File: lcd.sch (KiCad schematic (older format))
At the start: 1 part

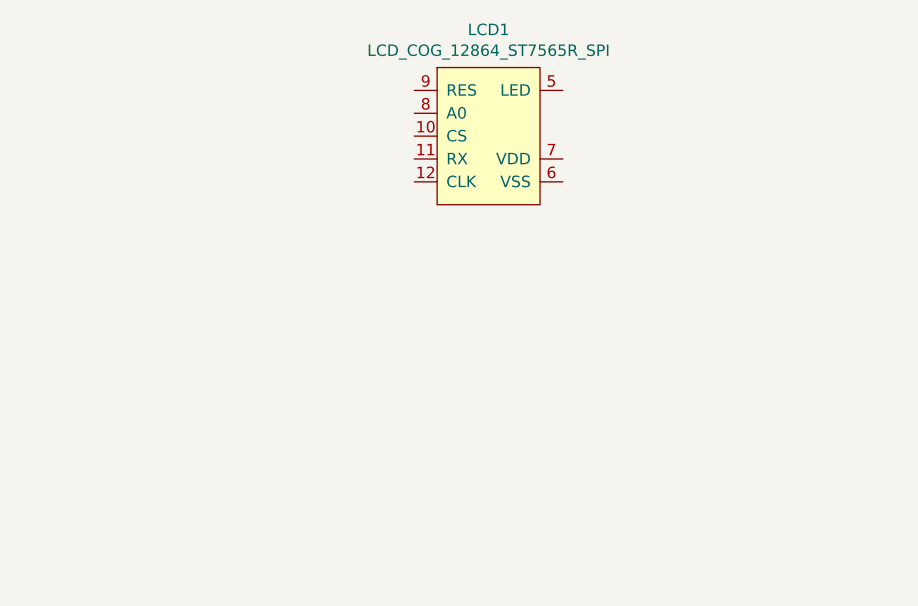
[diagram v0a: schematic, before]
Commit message: dcdc доделан на 5V.
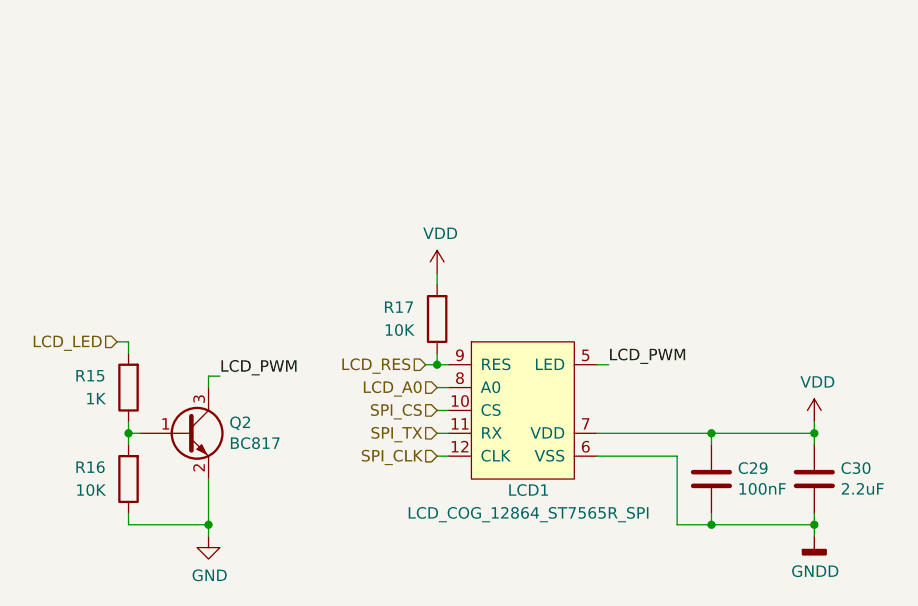
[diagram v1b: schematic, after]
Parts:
- added C29: 100nF, Capacitor_SMD:C_0603_1608Metric_Pad1.05x0.95mm_HandSolder, symbol Device:C
- added C30: 2.2uF, Capacitor_SMD:C_1206_3216Metric_Pad1.42x1.75mm_HandSolder, symbol Device:C
- added Q2: BC817, Package_TO_SOT_SMD:SOT-23, symbol Transistor_BJT:BC817
- added R15: 1K, Resistor_SMD:R_0603_1608Metric_Pad1.05x0.95mm_HandSolder, symbol Device:R
- added R16, R17: 10K, Resistor_SMD:R_0603_1608Metric_Pad1.05x0.95mm_HandSolder, symbol Device:R
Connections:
- net SPI_CS: now reaches LCD1.10 (CS)
- net SPI_TX: now reaches LCD1.11 (RX)
- net SPI_CLK: now reaches LCD1.12 (CLK)
- net LCD_PWM: now reaches LCD1.5 (LED)
- net LCD_PWM: now also Q2.3 (C)
- net GNDD: now reaches LCD1.6 (VSS)
- net GNDD: now also C29.2, C30.2
- net VDD: now reaches LCD1.7 (VDD)
- net VDD: now also C29.1, C30.1, R17.2
- net LCD_A0: now reaches LCD1.8 (A0)
- net LCD_RES: now reaches LCD1.9 (RES)
- net LCD_RES: now also R17.1
- new net: Q2.1 (B), R15.1, R16.2
- new net GND: Q2.2 (E), R16.1
- new net LCD_LED: R15.2
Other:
- moved on the sheet: LCD1
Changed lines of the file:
@@
 L lcd:LCD_COG_12864_ST7565R_SPI LCD1
 U 1 1 5E9E07DE
-P 5850 2700
-F 0 "LCD1" H 5825 3165 50  0000 C CNN
-F 1 "LCD_COG_12864_ST7565R_SPI" H 5825 3074 50  0000 C CNN
-F 2 "lcd:LCD_COG_12864_ST7565R" H 5850 3050 50  0001 C CNN
-F 3 "" H 5850 3050 50  0001 C CNN
-	1    5850 2700
-	1    0    0    -1
-$EndComp
+P 6000 3900
+F 0 "LCD1" H 6000 3550 50  0000 C CNN
+F 1 "LCD_COG_12864_ST7565R_SPI" H 6000 3450 50  0000 C CNN
+F 2 "lcd:LCD_COG_12864_ST7565R" H 6000 4250 50  0001 C CNN
+F 3 "" H 6000 4250 50  0001 C CNN
+	1    6000 3900
+	1    0    0    -1
+$EndComp
+$Comp
+L Device:R R?
+U 1 1 5EA8F117
+P 4250 3800
+AR Path="/5EBBB05A/5EA8F117" Ref="R?"  Part="1"
+AR Path="/5E9E00DA/5EA8F117" Ref="R15"  Part="1"
+F 0 "R15" H 4350 3750 50  0000 L CNN
+F 1 "1K" H 4350 3850 50  0000 L CNN
+F 2 "Resistor_SMD:R_0603_1608Metric_Pad1.05x0.95mm_HandSolder" V 4180 3800 50  0001 C CNN
+F 3 "~" H 4250 3800 50  0001 C CNN
+	1    4250 3800
+	-1   0    0    1
+$EndComp
+$Comp
+L Device:R R?
+U 1 1 5EA8F11D
+P 4250 4200
+AR Path="/5EBBB05A/5EA8F11D" Ref="R?"  Part="1"
+AR Path="/5E9E00DA/5EA8F11D" Ref="R16"  Part="1"
+F 0 "R16" H 4350 4150 50  0000 L CNN
+F 1 "10K" H 4350 4250 50  0000 L CNN
+F 2 "Resistor_SMD:R_0603_1608Metric_Pad1.05x0.95mm_HandSolder" V 4180 4200 50  0001 C CNN
+F 3 "~" H 4250 4200 50  0001 C CNN
+	1    4250 4200
+	-1   0    0    1
+$EndComp
+$Comp
+L Transistor_BJT:BC817 Q?
+U 1 1 5EA8F129
+P 4500 4000
+AR Path="/5EBBB05A/5EA8F129" Ref="Q?"  Part="1"
+AR Path="/5E9E00DA/5EA8F129" Ref="Q2"  Part="1"
+F 0 "Q2" H 4691 4046 50  0000 L CNN
+F 1 "BC817" H 4691 3955 50  0000 L CNN
+F 2 "Package_TO_SOT_SMD:SOT-23" H 4700 3925 50  0001 L CIN
+F 3 "http://www.fairchildsemi.com/ds/BC/BC817.pdf" H 4500 4000 50  0001 L CNN
+	1    4500 4000
+	1    0    0    -1
+$EndComp
+Wire Wire Line
+	4300 4000 4250 4000
+Wire Wire Line
+	4250 4000 4250 3950
+Wire Wire Line
+	4250 4050 4250 4000
+Connection ~ 4250 4000
+$Comp
+L power:GND #PWR?
+U 1 1 5EA8F142
+P 4600 4450
+AR Path="/5EBBB05A/5EA8F142" Ref="#PWR?"  Part="1"
+AR Path="/5E9E00DA/5EA8F142" Ref="#PWR042"  Part="1"
+F 0 "#PWR042" H 4600 4200 50  0001 C CNN
+F 1 "GND" H 4605 4277 50  0000 C CNN
+F 2 "" H 4600 4450 50  0001 C CNN
+F 3 "" H 4600 4450 50  0001 C CNN
+	1    4600 4450
+	1    0    0    -1
+$EndComp
+Wire Wire Line
+	4600 4200 4600 4400
+Wire Wire Line
+	4250 4350 4250 4400
+Wire Wire Line
+	4200 3600 4250 3600
+Wire Wire Line
+	4250 3600 4250 3650
+Wire Wire Line
+	4250 4400 4600 4400
+Wire Wire Line
+	4600 4400 4600 4450
+Connection ~ 4600 4400
+$Comp
+L Device:R R?
+U 1 1 5EA8F3E7
+P 5600 3500
+AR Path="/5EBBB05A/5EA8F3E7" Ref="R?"  Part="1"
+AR Path="/5E9E00DA/5EA8F3E7" Ref="R17"  Part="1"
+F 0 "R17" H 5700 3450 50  0000 L CNN
+F 1 "10K" H 5700 3550 50  0000 L CNN
+F 2 "Resistor_SMD:R_0603_1608Metric_Pad1.05x0.95mm_HandSolder" V 5530 3500 50  0001 C CNN
+F 3 "~" H 5600 3500 50  0001 C CNN
+	1    5600 3500
+	-1   0    0    1
+$EndComp
+Wire Wire Line
+	5600 3650 5600 3700
+Wire Wire Line
+	5600 3700 5650 3700
+Wire Wire Line
+	5600 3700 5550 3700
+Connection ~ 5600 3700
+Text HLabel 5550 3700 0    50   Input ~ 0
+LCD_RES
+Text HLabel 5600 3800 0    50   Input ~ 0
+LCD_A0
+Text HLabel 5600 4000 0    50   Input ~ 0
+SPI_TX
+Text HLabel 5600 4100 0    50   Input ~ 0
+SPI_CLK
+Text HLabel 5600 3900 0    50   Input ~ 0
+SPI_CS
+Wire Wire Line
+	5600 3800 5650 3800
+Wire Wire Line
+	5650 3900 5600 3900
+Wire Wire Line
+	5600 4000 5650 4000
+Wire Wire Line
+	5650 4100 5600 4100
+Wire Wire Line
+	6300 3700 6350 3700
+Text Label 6350 3700 0    50   ~ 0
+LCD_PWM
+$Comp
+L Device:C C29
+U 1 1 5EA92397
+P 6800 4200
+F 0 "C29" H 6915 4246 50  0000 L CNN
+F 1 "100nF" H 6915 4155 50  0000 L CNN
+F 2 "Capacitor_SMD:C_0603_1608Metric_Pad1.05x0.95mm_HandSolder" H 6838 4050 50  0001 C CNN
+F 3 "~" H 6800 4200 50  0001 C CNN
+	1    6800 4200
+	1    0    0    -1
+$EndComp
+$Comp
+L Device:C C30
+U 1 1 5EA9355E
+P 7250 4200
+F 0 "C30" H 7365 4246 50  0000 L CNN
+F 1 "2.2uF" H 7365 4155 50  0000 L CNN
+F 2 "Capacitor_SMD:C_1206_3216Metric_Pad1.42x1.75mm_HandSolder" H 7288 4050 50  0001 C CNN
+F 3 "~" H 7250 4200 50  0001 C CNN
+	1    7250 4200
+	1    0    0    -1
+$EndComp
+Wire Wire Line
+	6800 4000 6800 4050
+Wire Wire Line
+	6800 4000 7250 4000
+Wire Wire Line
+	7250 4000 7250 4050
+Connection ~ 6800 4000
+Wire Wire Line
+	6650 4100 6650 4400
+Wire Wire Line
+	6650 4400 6800 4400
+Wire Wire Line
+	6800 4400 6800 4350
+Wire Wire Line
+	6800 4400 7250 4400
+Wire Wire Line
+	7250 4400 7250 4350
+Connection ~ 6800 4400
+Wire Wire Line
+	6300 4100 6650 4100
+Wire Wire Line
+	6300 4000 6800 4000
+Wire Wire Line
+	7250 3950 7250 4000
+Connection ~ 7250 4000
+Wire Wire Line
+	7250 4400 7250 4450
+Connection ~ 7250 4400
+Wire Wire Line
+	4600 3800 4600 3750
+Wire Wire Line
+	4600 3750 4650 3750
+Text Label 4650 3750 0    50   ~ 0
+LCD_PWM
+Text HLabel 4200 3600 0    50   Input ~ 0
+LCD_LED
+Wire Wire Line
+	5600 3300 5600 3350
+$Comp
+L power:VDD #PWR?
+U 1 1 5EAD3F62
+P 5600 3300
+AR Path="/5EB7312D/5EAD3F62" Ref="#PWR?"  Part="1"
+AR Path="/5EAD3F62" Ref="#PWR?"  Part="1"
+AR Path="/5E9E00DA/5EAD3F62" Ref="#PWR0105"  Part="1"
+F 0 "#PWR0105" H 5600 3150 50  0001 C CNN
+F 1 "VDD" H 5615 3473 50  0000 C CNN
+F 2 "" H 5600 3300 50  0001 C CNN
+F 3 "" H 5600 3300 50  0001 C CNN
+	1    5600 3300
+	1    0    0    -1
+$EndComp
+$Comp
+L power:GNDD #PWR?
+U 1 1 5EAD3F68
+P 7250 4450
+AR Path="/5EB7312D/5EAD3F68" Ref="#PWR?"  Part="1"
+AR Path="/5EAD3F68" Ref="#PWR?"  Part="1"
+AR Path="/5E9E00DA/5EAD3F68" Ref="#PWR0106"  Part="1"
+F 0 "#PWR0106" H 7250 4200 50  0001 C CNN
+F 1 "GNDD" H 7254 4295 50  0000 C CNN
+F 2 "" H 7250 4450 50  0001 C CNN
+F 3 "" H 7250 4450 50  0001 C CNN
+	1    7250 4450
+	1    0    0    -1
+$EndComp
+$Comp
+L power:VDD #PWR?
+U 1 1 5EAD5803
+P 7250 3950
+AR Path="/5EB7312D/5EAD5803" Ref="#PWR?"  Part="1"
+AR Path="/5EAD5803" Ref="#PWR?"  Part="1"
+AR Path="/5E9E00DA/5EAD5803" Ref="#PWR0107"  Part="1"
+F 0 "#PWR0107" H 7250 3800 50  0001 C CNN
+F 1 "VDD" H 7265 4123 50  0000 C CNN
+F 2 "" H 7250 3950 50  0001 C CNN
+F 3 "" H 7250 3950 50  0001 C CNN
+	1    7250 3950
+	1    0    0    -1
+$EndComp
